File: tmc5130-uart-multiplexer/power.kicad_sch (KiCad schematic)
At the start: 6 parts, among them Q301 MOSFET-P-CH-EN_60V_50A, Q302 MOSFET-N-CH-EN_100V_260mA, T301 TERM_BLK_HDR_2POS_90DEG_0.2IN

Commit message: tmc51x0-multiplexer-uart -> tmc5130-uart-multiplexer
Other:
- title: tmc51x0-multiplexer-uart -> tmc5130-uart-multiplexer
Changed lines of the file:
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@@
   (paper "A4")
   (title_block
-    (title "tmc51x0-multiplexer-uart")
+    (title "tmc5130-uart-multiplexer")
     (date "2024-07-10")
     (rev "1.0")
@@
     (pin "1")
     (instances
-      (project "tmc51x0-multiplexer-uart"
+      (project "tmc5130-uart-multiplexer"
         (path "/df2b2e89-e055-4140-95de-f1df723db034/c1dd8f61-494c-402f-8e59-08309c64fc3f"
           (reference "T301") (unit 1)
@@
     (pin "1")
     (instances
-      (project "tmc51x0-multiplexer-uart"
+      (project "tmc5130-uart-multiplexer"
         (path "/df2b2e89-e055-4140-95de-f1df723db034/c1dd8f61-494c-402f-8e59-08309c64fc3f"
           (reference "Q301") (unit 1)
@@
     (pin "1")
     (instances
-      (project "tmc51x0-multiplexer-uart"
+      (project "tmc5130-uart-multiplexer"
         (path "/df2b2e89-e055-4140-95de-f1df723db034/c1dd8f61-494c-402f-8e59-08309c64fc3f"
           (reference "#FLG0303") (unit 1)
@@
     (pin "1")
     (instances
-      (project "tmc51x0-multiplexer-uart"
+      (project "tmc5130-uart-multiplexer"
         (path "/df2b2e89-e055-4140-95de-f1df723db034/c1dd8f61-494c-402f-8e59-08309c64fc3f"
           (reference "R301") (unit 1)
@@
     (pin "1")
     (instances
-      (project "tmc51x0-multiplexer-uart"
+      (project "tmc5130-uart-multiplexer"
         (path "/df2b2e89-e055-4140-95de-f1df723db034/c1dd8f61-494c-402f-8e59-08309c64fc3f"
           (reference "#FLG0302") (unit 1)
@@
     (pin "2")
     (instances
-      (project "tmc51x0-multiplexer-uart"
+      (project "tmc5130-uart-multiplexer"
         (path "/df2b2e89-e055-4140-95de-f1df723db034/c1dd8f61-494c-402f-8e59-08309c64fc3f"
           (reference "D301") (unit 1)
@@
     (pin "1")
     (instances
-      (project "tmc51x0-multiplexer-uart"
+      (project "tmc5130-uart-multiplexer"
         (path "/df2b2e89-e055-4140-95de-f1df723db034/c1dd8f61-494c-402f-8e59-08309c64fc3f"
           (reference "#FLG0301") (unit 1)
@@
     (pin "2")
     (instances
-      (project "tmc51x0-multiplexer-uart"
+      (project "tmc5130-uart-multiplexer"
         (path "/df2b2e89-e055-4140-95de-f1df723db034/c1dd8f61-494c-402f-8e59-08309c64fc3f"
           (reference "R302") (unit 1)
@@
     (pin "2")
     (instances
-      (project "tmc51x0-multiplexer-uart"
+      (project "tmc5130-uart-multiplexer"
         (path "/df2b2e89-e055-4140-95de-f1df723db034/c1dd8f61-494c-402f-8e59-08309c64fc3f"
           (reference "Q302") (unit 1)

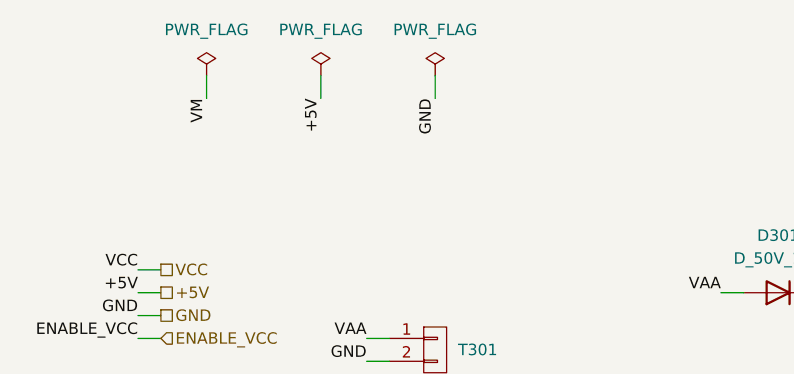
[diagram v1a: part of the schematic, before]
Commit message: Fix some design rule checks
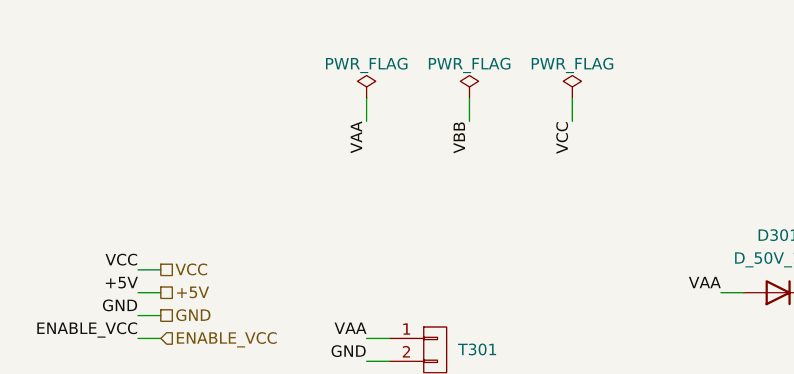
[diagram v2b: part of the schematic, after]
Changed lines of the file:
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@@
     (stroke (width 0) (type default))
   )
-  (wire (pts (xy 90.17 36.83) (xy 90.17 39.37))
-    (stroke (width 0) (type default))
-  )
-  (wire (pts (xy 77.47 36.83) (xy 77.47 39.37))
+  (wire (pts (xy 105.41 39.37) (xy 105.41 41.91))
     (stroke (width 0) (type default))
   )
@@
     (stroke (width 0) (type default))
   )
+  (wire (pts (xy 82.55 39.37) (xy 82.55 41.91))
+    (stroke (width 0) (type default))
+  )
+  (wire (pts (xy 93.98 39.37) (xy 93.98 41.91))
+    (stroke (width 0) (type default))
+  )
   (wire (pts (xy 59.69 60.96) (xy 57.15 60.96))
     (stroke (width 0) (type default))
@@
     (stroke (width 0) (type default))
   )
-  (wire (pts (xy 64.77 36.83) (xy 64.77 39.37))
-    (stroke (width 0) (type default))
-  )
   (wire (pts (xy 115.57 95.25) (xy 115.57 92.71))
     (stroke (width 0) (type default))
@@
     (stroke (width 0) (type default))
   )
+  (label "VAA" (at 82.55 41.91 270) (fields_autoplaced)
+    (effects (font (size 1.27 1.27)) (justify right bottom))
+  )
   (label "~{ENABLE_VCC}" (at 151.13 109.22 180) (fields_autoplaced)
     (effects (font (size 1.27 1.27)) (justify right bottom))
   )
   (label "VAA" (at 121.92 60.96 180) (fields_autoplaced)
-    (effects (font (size 1.27 1.27)) (justify right bottom))
-  )
-  (label "GND" (at 90.17 39.37 270) (fields_autoplaced)
     (effects (font (size 1.27 1.27)) (justify right bottom))
   )
@@
     (effects (font (size 1.27 1.27)) (justify left bottom))
   )
+  (label "VBB" (at 93.98 41.91 270) (fields_autoplaced)
+    (effects (font (size 1.27 1.27)) (justify right bottom))
+  )
   (label "VCC" (at 57.15 58.42 180) (fields_autoplaced)
     (effects (font (size 1.27 1.27)) (justify right bottom))
   )
-  (label "VM" (at 64.77 39.37 270) (fields_autoplaced)
+  (label "VCC" (at 105.41 41.91 270) (fields_autoplaced)
     (effects (font (size 1.27 1.27)) (justify right bottom))
   )
@@
   )
   (label "ENABLE_VCC" (at 57.15 66.04 180) (fields_autoplaced)
-    (effects (font (size 1.27 1.27)) (justify right bottom))
-  )
-  (label "+5V" (at 77.47 39.37 270) (fields_autoplaced)
     (effects (font (size 1.27 1.27)) (justify right bottom))
   )
@@
     )
   )
+  (symbol (lib_id "power:PWR_FLAG") (at 82.55 39.37 0) (unit 1)
+    (in_bom yes) (on_board yes) (dnp no)
+    (property "Reference" "#FLG0301" (at 82.55 37.465 0)
+      (effects (font (size 1.27 1.27)) hide)
+    )
+    (property "Value" "PWR_FLAG" (at 82.55 35.56 0)
+      (effects (font (size 1.27 1.27)))
+    )
+    (property "Footprint" "" (at 82.55 39.37 0)
+      (effects (font (size 1.27 1.27)) hide)
+    )
+    (property "Datasheet" "~" (at 82.55 39.37 0)
+      (effects (font (size 1.27 1.27)) hide)
+    )
+    (pin "1")
+    (instances
+      (project "tmc5130-uart-multiplexer"
+        (path "/df2b2e89-e055-4140-95de-f1df723db034/c1dd8f61-494c-402f-8e59-08309c64fc3f"
+          (reference "#FLG0301") (unit 1)
+        )
+      )
+    )
+  )
   (symbol (lib_id "Janelia:MOSFET-P-CH-EN_60V_50A") (at 158.75 109.22 0) (unit 1)
     (in_bom yes) (on_board yes) (dnp no) (fields_autoplaced)
@@
     )
   )
-  (symbol (lib_id "power:PWR_FLAG") (at 90.17 36.83 0) (unit 1)
-    (in_bom yes) (on_board yes) (dnp no) (fields_autoplaced)
-    (property "Reference" "#FLG0303" (at 90.17 34.925 0)
-      (effects (font (size 1.27 1.27)) hide)
-    )
-    (property "Value" "PWR_FLAG" (at 90.17 31.75 0)
+  (symbol (lib_id "power:PWR_FLAG") (at 93.98 39.37 0) (unit 1)
+    (in_bom yes) (on_board yes) (dnp no)
+    (property "Reference" "#FLG0302" (at 93.98 37.465 0)
+      (effects (font (size 1.27 1.27)) hide)
+    )
+    (property "Value" "PWR_FLAG" (at 93.98 35.56 0)
       (effects (font (size 1.27 1.27)))
     )
-    (property "Footprint" "" (at 90.17 36.83 0)
-      (effects (font (size 1.27 1.27)) hide)
-    )
-    (property "Datasheet" "~" (at 90.17 36.83 0)
-      (effects (font (size 1.27 1.27)) hide)
-    )
-    (pin "1")
-    (instances
-      (project "tmc5130-uart-multiplexer"
-        (path "/df2b2e89-e055-4140-95de-f1df723db034/c1dd8f61-494c-402f-8e59-08309c64fc3f"
-          (reference "#FLG0303") (unit 1)
+    (property "Footprint" "" (at 93.98 39.37 0)
+      (effects (font (size 1.27 1.27)) hide)
+    )
+    (property "Datasheet" "~" (at 93.98 39.37 0)
+      (effects (font (size 1.27 1.27)) hide)
+    )
+    (pin "1")
+    (instances
+      (project "tmc5130-uart-multiplexer"
+        (path "/df2b2e89-e055-4140-95de-f1df723db034/c1dd8f61-494c-402f-8e59-08309c64fc3f"
+          (reference "#FLG0302") (unit 1)
         )
       )
@@
     )
   )
-  (symbol (lib_id "power:PWR_FLAG") (at 77.47 36.83 0) (unit 1)
-    (in_bom yes) (on_board yes) (dnp no) (fields_autoplaced)
-    (property "Reference" "#FLG0302" (at 77.47 34.925 0)
-      (effects (font (size 1.27 1.27)) hide)
-    )
-    (property "Value" "PWR_FLAG" (at 77.47 31.75 0)
-      (effects (font (size 1.27 1.27)))
-    )
-    (property "Footprint" "" (at 77.47 36.83 0)
-      (effects (font (size 1.27 1.27)) hide)
-    )
-    (property "Datasheet" "~" (at 77.47 36.83 0)
-      (effects (font (size 1.27 1.27)) hide)
-    )
-    (pin "1")
-    (instances
-      (project "tmc5130-uart-multiplexer"
-        (path "/df2b2e89-e055-4140-95de-f1df723db034/c1dd8f61-494c-402f-8e59-08309c64fc3f"
-          (reference "#FLG0302") (unit 1)
-        )
-      )
-    )
-  )
   (symbol (lib_id "Janelia:D_50V_15A") (at 128.27 60.96 180) (unit 1)
     (in_bom yes) (on_board yes) (dnp no) (fields_autoplaced)
@@
     )
   )
-  (symbol (lib_id "power:PWR_FLAG") (at 64.77 36.83 0) (unit 1)
-    (in_bom yes) (on_board yes) (dnp no) (fields_autoplaced)
-    (property "Reference" "#FLG0301" (at 64.77 34.925 0)
-      (effects (font (size 1.27 1.27)) hide)
-    )
-    (property "Value" "PWR_FLAG" (at 64.77 31.75 0)
-      (effects (font (size 1.27 1.27)))
-    )
-    (property "Footprint" "" (at 64.77 36.83 0)
-      (effects (font (size 1.27 1.27)) hide)
-    )
-    (property "Datasheet" "~" (at 64.77 36.83 0)
-      (effects (font (size 1.27 1.27)) hide)
-    )
-    (pin "1")
-    (instances
-      (project "tmc5130-uart-multiplexer"
-        (path "/df2b2e89-e055-4140-95de-f1df723db034/c1dd8f61-494c-402f-8e59-08309c64fc3f"
-          (reference "#FLG0301") (unit 1)
-        )
-      )
-    )
-  )
   (symbol (lib_id "Janelia:R_3.6k_0402") (at 115.57 116.84 0) (unit 1)
     (in_bom yes) (on_board yes) (dnp no)
@@
         )
       )
+    )
+  )
+  (symbol (lib_id "power:PWR_FLAG") (at 105.41 39.37 0) (unit 1)
+    (in_bom yes) (on_board yes) (dnp no)
+    (property "Reference" "#FLG0303" (at 105.41 37.465 0)
+      (effects (font (size 1.27 1.27)) hide)
+    )
+    (property "Value" "PWR_FLAG" (at 105.41 35.56 0)
+      (effects (font (size 1.27 1.27)))
+    )
+    (property "Footprint" "" (at 105.41 39.37 0)
+      (effects (font (size 1.27 1.27)) hide)
+    )
+    (property "Datasheet" "~" (at 105.41 39.37 0)
+      (effects (font (size 1.27 1.27)) hide)
+    )
+    (pin "1")
+    (instances
+      (project "tmc5130-uart-multiplexer"
+        (path "/df2b2e89-e055-4140-95de-f1df723db034/c1dd8f61-494c-402f-8e59-08309c64fc3f"
+          (reference "#FLG0303") (unit 1)
+        )
+      )
